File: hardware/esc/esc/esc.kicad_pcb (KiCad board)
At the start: 4 copper layers, 120 x 80 mm, 298 parts, among them IC1 IR2136SPBF, IC2 IR2136SPBF, IC3 IR2136SPBF, IC4 IR2136SPBF, IC5 IR2136SPBF, IC6 IR2136SPBF, IC7 TLA2528IRTER, IC8 MP9486AGN-Z, J1 USB-C, J10 GPIO, J11 Conn_01x08_Pin, J2 DEBUG, J3 TEMP-GPIO, Q1 NMOS, Q10 NMOS, Q11 NMOS, Q12 NMOS, Q13 NMOS, Q14 NMOS, Q15 NMOS, Q16 NMOS, Q17 NMOS, Q18 NMOS, Q19 NMOS, Q2 NMOS, Q20 NMOS, Q21 NMOS, Q22 NMOS, Q23 NMOS, Q24 NMOS, Q25 NMOS, Q26 NMOS, Q27 NMOS, Q28 NMOS, Q29 NMOS, Q3 NMOS, Q30 NMOS, Q31 NMOS, Q32 NMOS, Q33 NMOS, Q34 NMOS, Q35 NMOS, Q36 NMOS, Q4 NMOS, Q5 NMOS, Q6 NMOS, Q7 NMOS, Q8 NMOS, Q9 NMOS, SW1 SW_Push, SW2 SW_Push, U1 RP2354B, U10 INA240A2PW, U11 INA240A2PW, U12 INA240A2PW, U14 TMP110D, U15 TMP110D, U16 AZ1117CH2-3.3, U2 INA240A2PW, U3 INA240A2PW, U4 INA240A2PW, U5 INA240A2PW, U6 INA240A2PW, U7 INA240A2PW, U8 INA240A2PW, U9 INA240A2PW, Y1 12MHz

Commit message: row 1 done
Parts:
- moved R22 213.4 mm to (107.3, 2.22), turned to 90 degrees
- moved R21 211.1 mm to (117.7, 28.9), turned to 180 degrees
- moved R23 209.2 mm to (107.3, 10.0), turned to 90 degrees
- moved R20 206.4 mm to (117.7, 31.2), turned to 180 degrees
- moved R19 201.7 mm to (117.8, 33.5), turned to 180 degrees
- moved R18 199.6 mm to (102.6, 1.21), turned to 180 degrees
- moved C14 198.6 mm to (106.7, 5.42), turned to -90 degrees
- moved R12 191.4 mm to (99.7, 21.1), turned to 90 degrees
- moved R6 191.2 mm to (83.3, 13.9), turned to 90 degrees
- moved R11 187.4 mm to (97.4, 21.1), turned to 90 degrees
- moved R5 184.0 mm to (67.7, 13.9), turned to 90 degrees
- moved R10 183.3 mm to (95.1, 21.1), turned to 90 degrees
- moved TP6 183.3 mm to (58.1, 2.29), turned to 90 degrees
- moved C6 181.3 mm to (55.3, 12.3), turned to 180 degrees
- moved R9 180.6 mm to (55.6, 13.9)
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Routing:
- net +3V3: track 69.0 -> 195.3 mm, vias 0 -> 5
- net Net-(U4-+): track 0.00 -> 77.1 mm, vias 0 -> 88
- net Net-(IC2-VB3): track 0.00 -> 60.6 mm, vias 0 -> 2
- net Net-(IC2-VS3): track 0.00 -> 58.9 mm, vias 0 -> 2
- net Net-(IC1-HO1): track 0.00 -> 57.1 mm
- net Net-(IC1-ITRIP): track 0.00 -> 54.5 mm
- net Net-(IC1-VB1): track 0.00 -> 51.9 mm
- net Net-(IC1-VS1): track 0.00 -> 49.0 mm
- net Net-(IC2-LO1): track 0.00 -> 48.0 mm, vias 0 -> 2
- net Net-(IC2-VS1): track 0.00 -> 45.3 mm
- net Net-(U2-+): track 0.00 -> 43.7 mm, vias 0 -> 90
- net Net-(IC2-HO3): track 0.00 -> 41.4 mm, vias 0 -> 2
- net Net-(IC2-LO2): track 0.00 -> 36.8 mm, vias 0 -> 2
- net Net-(IC1-VB2): track 0.00 -> 35.0 mm
- net Net-(IC2-LO3): track 0.00 -> 32.7 mm, vias 0 -> 2
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- added copper zone on F.Cu, net Net-(IC1-VS1)
- added copper zone on F.Cu, net Net-(IC1-VS2)
- added copper zone on F.Cu, net Net-(IC1-VS3)
- added copper zone on F.Cu, net Net-(IC2-VS1)
- added copper zone on F.Cu, net Net-(IC2-VS2)
- added copper zone on F.Cu, net Net-(IC2-VS3)
- added copper zone on F.Cu, net Net-(U2-+)
- added copper zone on In1.Cu, net Net-(U2-+)
- added copper zone on F.Cu, net Net-(U4-+)
- added copper zone on In1.Cu, net Net-(U4-+)

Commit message: block 2z1
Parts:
- moved C42 172.2 mm to (4.17, 55.9), turned to 180 degrees
- moved R88 157.2 mm to (5.34, 61.1), turned to -90 degrees
- moved R89 152.0 mm to (20.2, 60.5), turned to 180 degrees
- moved U12 147.9 mm to (15.4, 58.9), turned to 90 degrees
- moved R90 147.2 mm to (36.5, 60.4), turned to -90 degrees
- moved D17 143.3 mm to (2.62, 65.0), turned to -90 degrees
- moved C36 142.3 mm to (10.4, 65.9)
- moved U11 141.0 mm to (30.8, 57.6), turned to 90 degrees
- moved C38 140.2 mm to (25.9, 66.1)
- moved R80 139.3 mm to (21.6, 66.2), turned to -90 degrees
- moved C37 134.4 mm to (40.5, 66.1)
- moved R79 134.3 mm to (37.1, 66.1), turned to -90 degrees
- moved U10 130.4 mm to (47.5, 61.4), turned to 90 degrees
- moved R84 129.4 mm to (13.8, 66.1), turned to -90 degrees
- moved D16 128.8 mm to (18.6, 65.0), turned to -90 degrees
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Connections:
- C40 pad 1: Net-(IC6-VB1) -> Net-(IC6-VS1)
- C40 pad 2: Net-(IC6-VS1) -> Net-(IC6-VB1)
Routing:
- net Net-(IC6-VS1): track 0.00 -> 51.8 mm
- net Net-(IC6-LO3): track 0.00 -> 50.7 mm, vias 0 -> 2
- net Net-(IC6-VB1): track 0.00 -> 48.5 mm
- net Net-(IC6-HO1): track 0.00 -> 37.9 mm, vias 0 -> 2
- net Net-(IC6-VB2): track 0.00 -> 37.0 mm, vias 0 -> 2
- net Net-(IC6-VS2): track 0.00 -> 33.9 mm, vias 0 -> 2
- net Net-(IC6-VB3): track 0.00 -> 29.0 mm
- net Net-(IC6-VS3): track 0.00 -> 28.1 mm
- net Net-(IC6-HO2): track 0.00 -> 26.9 mm, vias 0 -> 2
- net Net-(IC6-LO2): track 0.00 -> 25.0 mm
- net Net-(IC6-HO3): track 0.00 -> 21.8 mm
- net Net-(IC6-LO1): track 0.00 -> 14.0 mm
- net Net-(U11-+): track 0.00 -> 11.3 mm
- net Net-(U12-+): track 0.00 -> 9.99 mm
- net Net-(U10-+): track 0.00 -> 7.91 mm
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
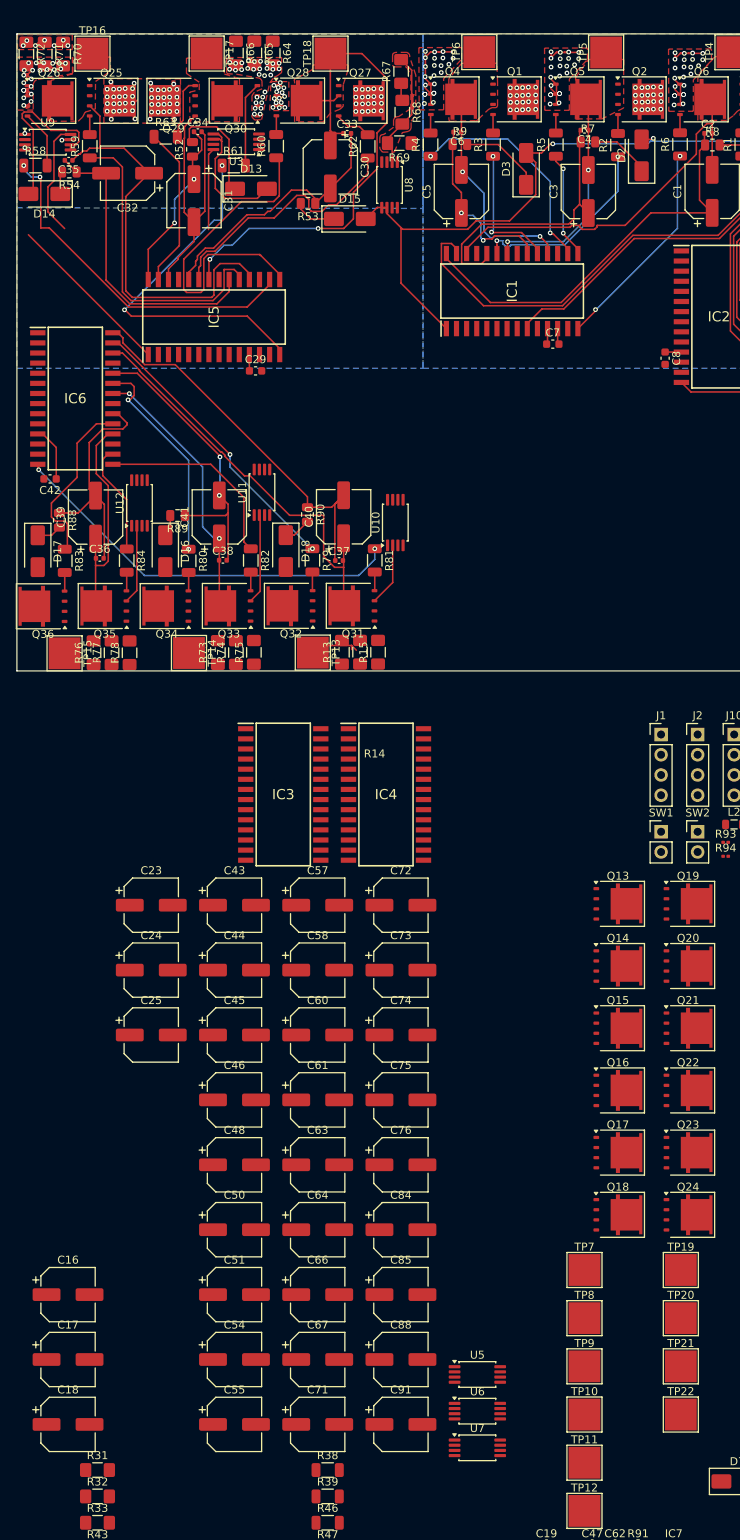
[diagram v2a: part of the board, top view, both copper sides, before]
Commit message: row 1 done for real, via density updated
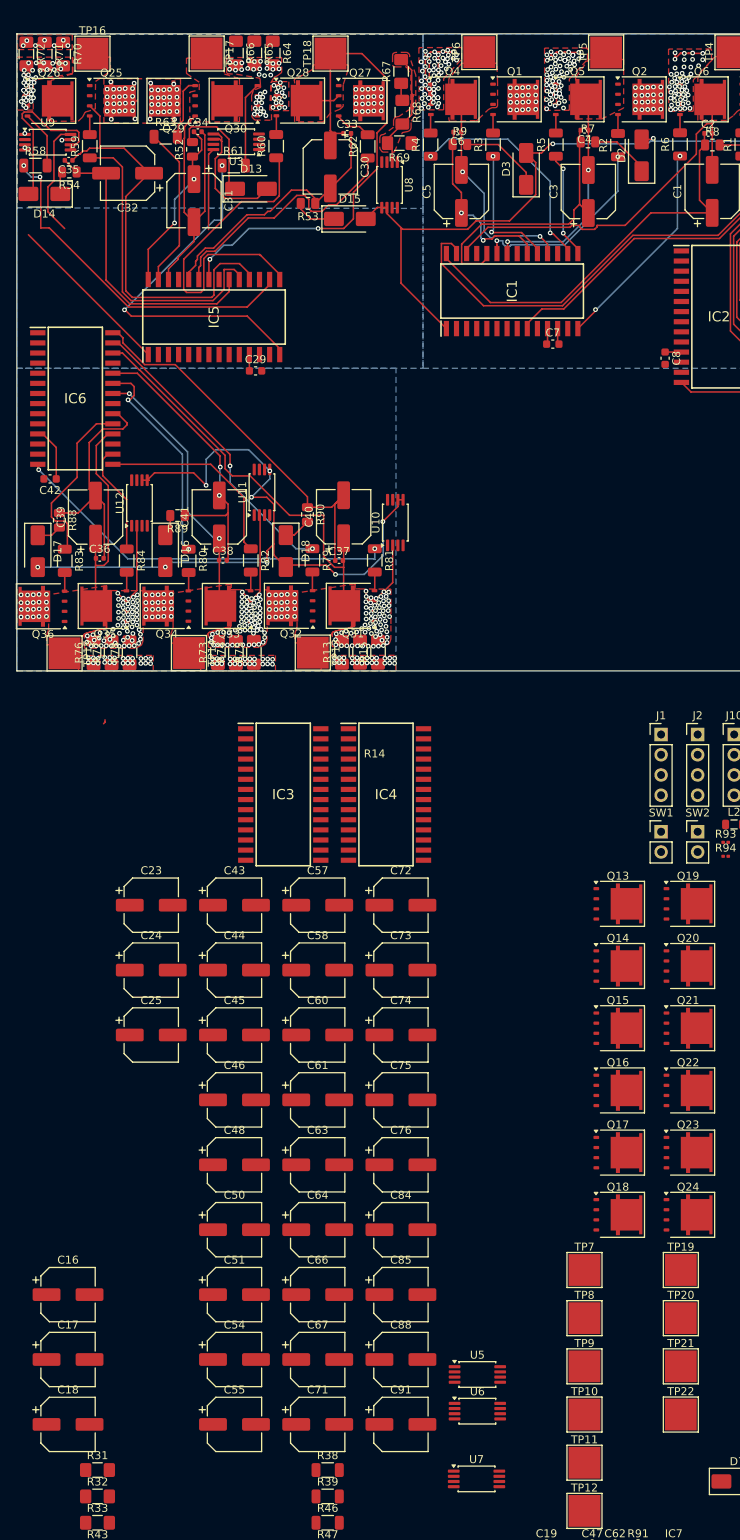
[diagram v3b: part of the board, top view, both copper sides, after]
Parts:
- moved U7 3.91 mm to (57.7, 181.5)
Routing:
- net +3V3: track 195.3 -> 282.1 mm, vias 5 -> 13
- net Net-(U2-+): track 43.7 -> 87.0 mm, vias 90 -> 188
- net Net-(U10-+): track 7.91 -> 9.91 mm, vias 0 -> 66
- net Net-(U9-+): track 19.4 -> 21.0 mm, vias 22 -> 36
- net Net-(IC6-LO3): track 50.7 -> 49.1 mm
- net Net-(U11-+): track 11.3 -> 12.9 mm, vias 0 -> 62
- net Net-(U12-+): track 9.99 -> 11.5 mm, vias 0 -> 64
- net Net-(IC6-HO1): track 37.9 -> 39.1 mm
- net GND: track 18.9 -> 20.0 mm, vias 48 -> 120
- net Net-(IC6-VS1): track 51.8 -> 52.6 mm
- net Net-(U3-+): vias 30 -> 35
- net +BATT: vias 188 -> 248
- added copper zone on F.Cu, net Net-(IC6-VS1)
- added copper zone on F.Cu, net Net-(IC6-VS2)
- added copper zone on F.Cu, net Net-(IC6-VS3)
- added copper zone on F.Cu, net Net-(U10-+)
- added copper zone on In1.Cu, net Net-(U10-+)
- added copper zone on F.Cu, net Net-(U11-+)
- added copper zone on In1.Cu, net Net-(U11-+)
- added copper zone on F.Cu, net Net-(U12-+)
- added copper zone on In1.Cu, net Net-(U12-+)

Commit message: block 2x2
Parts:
- moved C18 141.8 mm to (82.1, 54.6), turned to 90 degrees
- moved R33 137.2 mm to (91.5, 76.5)
- moved C17 130.6 mm to (73.9, 54.6), turned to 90 degrees
- moved C16 119.5 mm to (65.8, 54.6), turned to 90 degrees
- moved R39 118.4 mm to (54.0, 66.2), turned to -90 degrees
- moved R38 118.2 mm to (69.5, 66.2), turned to -90 degrees
- moved R32 117.7 mm to (63.3, 78.7), turned to 180 degrees
- moved R31 116.7 mm to (63.3, 76.5), turned to 180 degrees
- moved U5 92.6 mm to (77.6, 77.8)
- moved TP9 90.5 mm to (85.2, 77.9)
- moved TP8 83.5 mm to (69.6, 77.8)
- moved TP7 79.3 mm to (54.0, 77.8)
- moved Q18 78.1 mm to (59.0, 71.9), turned to 180 degrees
- moved Q17 72.7 mm to (51.3, 71.9), turned to 180 degrees
- moved Q16 60.8 mm to (74.6, 71.9), turned to 180 degrees
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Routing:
- net +3V3: track 282.1 -> 287.2 mm
- net +BATT: vias 248 -> 308

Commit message: block 2x2 zoing updates
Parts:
- moved R28 148.6 mm to (53.2, 58.9), turned to -90 degrees
- moved R36 141.0 mm to (77.3, 66.2), turned to -90 degrees
- moved R34 140.6 mm to (93.0, 66.3), turned to -90 degrees
- moved R35 140.5 mm to (85.2, 66.2), turned to -90 degrees
- moved R37 140.2 mm to (61.8, 66.2), turned to -90 degrees
- moved U1 137.0 mm to (41.4, 35.9)
- moved R30 129.8 mm to (84.6, 58.9), turned to -90 degrees
- moved C21 129.5 mm to (89.6, 66.0)
- moved R29 129.0 mm to (69.0, 58.8), turned to -90 degrees
- moved C20 125.8 mm to (58.4, 66.0), turned to 180 degrees
- moved C19 123.7 mm to (74.0, 66.0)
- moved D7 123.2 mm to (51.1, 65.0), turned to -90 degrees
- moved D9 99.3 mm to (66.7, 65.0), turned to -90 degrees
- moved D8 90.9 mm to (82.2, 65.0), turned to -90 degrees
- moved IC4 54.1 mm to (73.0, 48.4), turned to -90 degrees
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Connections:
- C17 pad 1: Net-(IC3-VB1) -> Net-(IC3-VS1)
- C17 pad 2: Net-(IC3-VS1) -> Net-(IC3-VB1)
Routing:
- net Net-(IC3-VS3): track 0.00 -> 59.1 mm
- net Net-(IC3-LO1): track 0.00 -> 57.8 mm
- net Net-(IC3-VB3): track 0.00 -> 52.5 mm, vias 0 -> 2
- net Net-(IC3-HO3): track 0.00 -> 43.9 mm, vias 0 -> 2
- net Net-(IC3-LO2): track 0.00 -> 38.4 mm, vias 0 -> 2
- net Net-(IC3-VS2): track 0.00 -> 36.1 mm
- net Net-(IC3-LO3): track 0.00 -> 34.5 mm
- net Net-(IC3-VS1): track 0.00 -> 28.5 mm, vias 0 -> 2
- net Net-(IC3-VB2): track 0.00 -> 27.5 mm, vias 0 -> 2
- net Net-(IC3-VB1): track 0.00 -> 21.7 mm, vias 0 -> 2
- net Net-(IC3-HO2): track 0.00 -> 20.8 mm, vias 0 -> 2
- net Net-(IC3-HO1): track 0.00 -> 18.2 mm, vias 0 -> 2
- net Net-(D9-K): track 0.00 -> 4.25 mm
- net Net-(D8-K): track 0.00 -> 4.14 mm
- net Net-(D7-K): track 0.00 -> 4.01 mm
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
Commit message: row 3 zoning in place
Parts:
- removed C76, C84, C85, C88, C91: 4.7uF, Capacitor_SMD:CP_Elec_6.3x7.7
- removed R55, R56, R57: SHUNT, Fuse:Fuse_1206_3216Metric_Pad1.42x1.75mm_HandSolder
- removed U7: INA240A2PW, Package_SO:TSSOP-8_4.4x3mm_P0.65mm
- added Q37: SMALL, Package_TO_SOT_SMD:SOT-23-3, F.Cu at (117.1, 77.6)
- added Q38: SMALL, Package_TO_SOT_SMD:SOT-23-3, F.Cu at (123.3, 85.3)
- C43, C46, C50, C57: value 4.7uF -> 1uF
- C48, C54, C55, C58, C63, C66, C71, C72, C73, C74, C75: value 4.7uF -> 10uF
- C60, C67: value 4.7uF -> 0.1uF; footprint Capacitor_SMD:CP_Elec_6.3x7.7 -> Capacitor_SMD:C_0603_1608Metric
- moved R45 175.6 mm to (117.8, 58.1), turned to 180 degrees
- moved R46 155.0 mm to (106.2, 47.4)
- moved C28 151.5 mm to (107.6, 53.5), turned to 180 degrees
- moved R47 150.9 mm to (106.2, 55.1)
- moved R50 150.3 mm to (104.9, 65.1), turned to -90 degrees
- moved R44 149.8 mm to (105.1, 77.7), turned to 90 degrees
- moved R51 148.8 mm to (99.1, 67.3)
- moved R43 148.7 mm to (107.4, 77.8), turned to 90 degrees
- moved R49 146.3 mm to (102.6, 65.1), turned to -90 degrees
- moved R48 145.6 mm to (107.5, 65.1), turned to 90 degrees
- moved R42 144.8 mm to (105.0, 53.0), turned to 180 degrees
- moved TP12 140.2 mm to (117.8, 53.2)
- moved C26 137.1 mm to (116.3, 67.7)
- moved R41 133.5 mm to (103.1, 61.3), turned to 180 degrees
- moved C27 125.4 mm to (97.1, 75.8)
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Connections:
- C60 pad 1: +3V3 -> GND
- C60 pad 2: GND -> +5V
- C63 pad 1: +3V3 -> +5V
- C66 pad 1: +3V3 -> +5V
- C67 pad 1: +3V3 -> GND
- C67 pad 2: GND -> +5V
- C73 pad 1: +5V -> GND
- C73 pad 2: GND -> +1V1
- C75 pad 1: +5V -> GND
- C75 pad 2: GND -> unconnected-(C75-Pad2)
- U1 pad 13: Net-(U1-GPIO14) -> Net-(Q37-G)
- U1 pad 14: Net-(U1-GPIO15) -> Net-(Q38-G)
- U14 pad 3: Net-(U1-GPIO14) -> Net-(Q37-D)
- U14 pad 5: +3V3 -> Net-(Q37-D)
- U15 pad 3: Net-(U1-GPIO15) -> Net-(Q38-D)
- U15 pad 5: +3V3 -> Net-(Q38-D)
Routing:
- net Net-(Q37-D): track 0.00 -> 7.13 mm
- net Net-(Q21-G): track 0.00 -> 6.92 mm, vias 0 -> 2
- net Net-(D11-K): track 0.00 -> 3.18 mm
- net Net-(D12-K): track 0.00 -> 3.07 mm
- net Net-(Q22-G): track 0.00 -> 2.86 mm
- net Net-(D10-K): track 0.00 -> 2.80 mm
- net Net-(Q23-G): track 0.00 -> 2.37 mm
- net Net-(Q20-G): track 0.00 -> 2.36 mm
- net Net-(Q19-G): track 0.00 -> 2.34 mm
- net Net-(IC4-VB3): track 0.00 -> 1.45 mm
- net Net-(IC4-VB1): track 0.00 -> 1.41 mm
- net Net-(Q24-G): track 0.00 -> 0.85 mm
- net Net-(U9-+): vias 36 -> 57
- net Net-(U8-+): vias 14 -> 65
- net Net-(U3-+): vias 35 -> 44
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- added copper zone on F.Cu, net Net-(IC4-VS1)
